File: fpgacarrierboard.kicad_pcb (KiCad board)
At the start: 6 copper layers, 150 x 100 mm, 211 parts, among them J1 Conn_01x06, J2 Conn_Coaxial, J3 HR911130C, J4 SFPK-SL, J5 Conn_02x10_Odd_Even, SW1 SW_Push, SW2 SW_Push, SW3 SW_Push, U1 TPS62130A, U2 TPS62130A, U3 TPS62130A, U4 TPS62130A, U5 TPS2592xx, U6 XC7A35T-FGG484, U7 W25Q128JVS, U8 RTL8211E-VB-CG, Y1 OT322550MJBA4SL, Y3 OT322525MJBA4SL

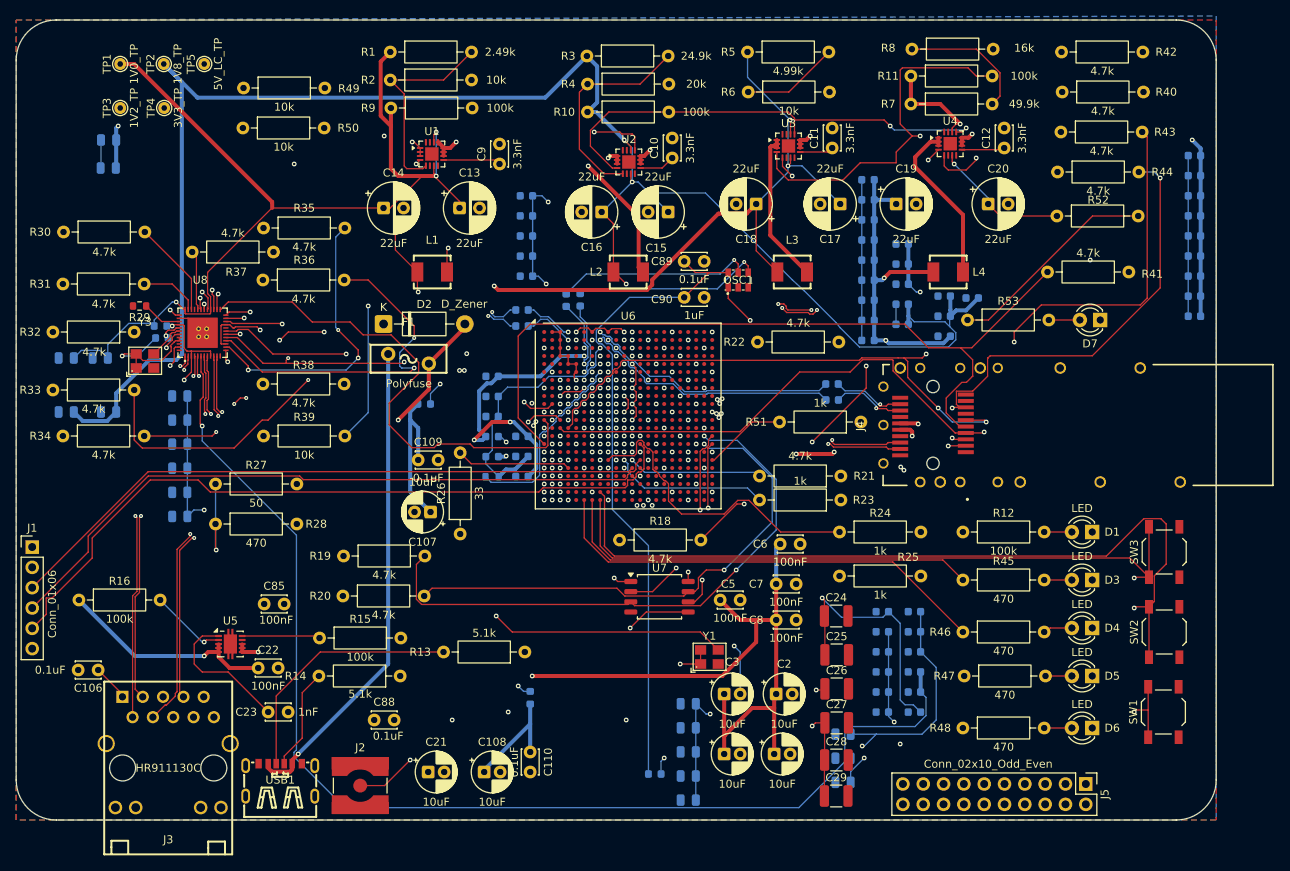
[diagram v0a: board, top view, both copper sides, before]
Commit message: As-ordered: fab outputs, JLC BOM/CPL, hand-solder BOM
- Gerbers and drill files (gerbers/), 6-layer, matching board saved 00:32
- bom_jlc.csv / gerbers/fpgacarrierboard-BOM.csv: 109 SMD parts for JLC
- gerbers/fpgacarrierboard-CPL.csv: placement for the same 109 parts
- bom_handsolder.csv: 97 through-hole parts plus SW1-SW3
- DRC: 0 errors, 0 unconnected, parity clean
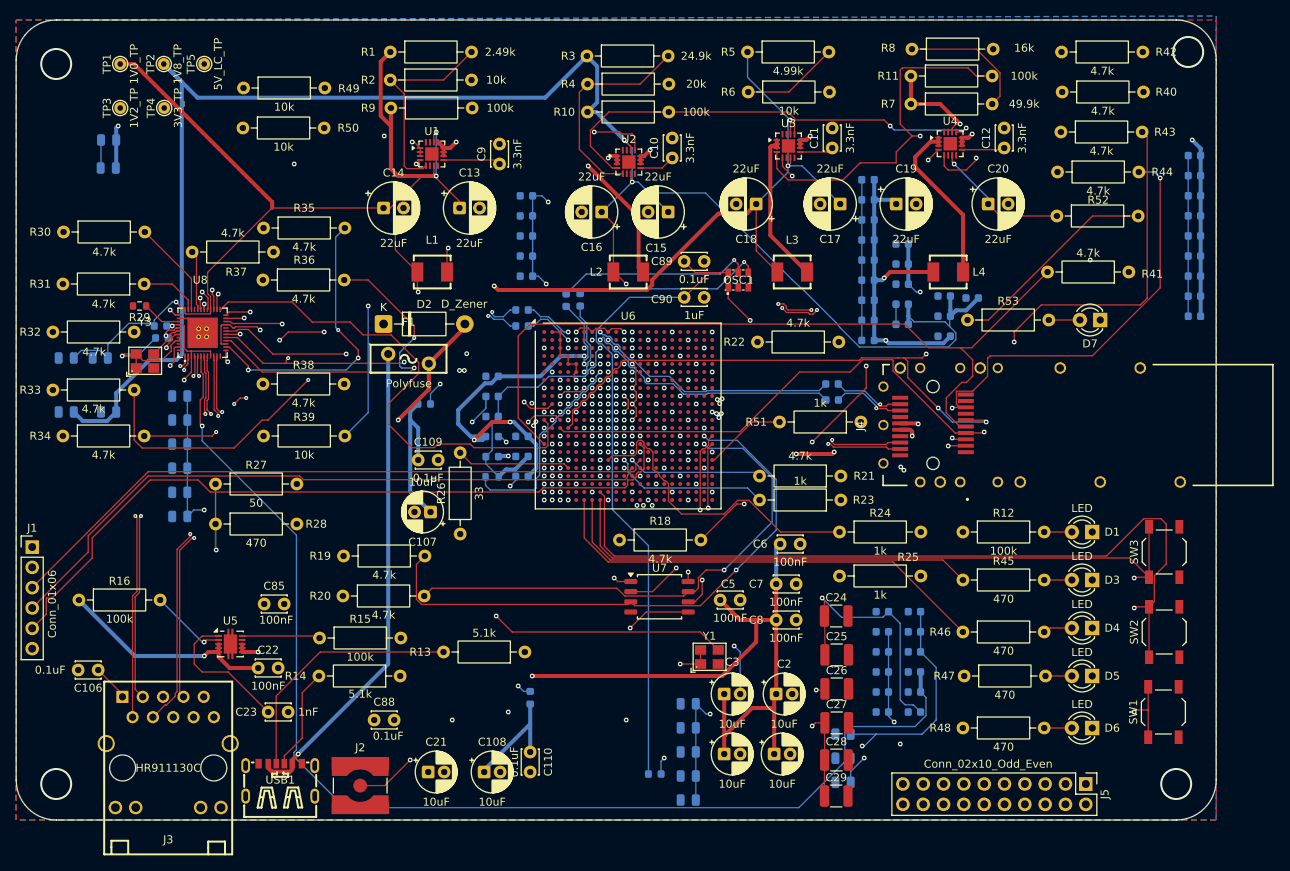
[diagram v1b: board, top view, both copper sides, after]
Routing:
- net GND: track 98.0 -> 117.3 mm, vias 109 -> 115
- net MGTAVCC: track 44.5 -> 48.0 mm
- net Net-(U6E-MGTRREF_216): track 24.8 -> 27.0 mm
- net 1V2: track 199.8 -> 200.3 mm
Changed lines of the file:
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@@
 			(outputformat 1)
 			(mirror no)
-			(drillshape 1)
+			(drillshape 0)
 			(scaleselection 1)
-			(outputdirectory "")
+			(outputdirectory "gerbers/")
 		)
 	)
@@
 	)
 	(via
-		(at 186.25 79)
+		(at 186.5 79)
 		(size 0.6)
 		(drill 0.3)
@@
 	)
 	(segment
-		(start 185.2775 79.08)
-		(end 186.17 79.08)
-		(width 0.5)
+		(start 221.475 43.525)
+		(end 217.5 47.5)
+		(width 0.15)
 		(layer "B.Cu")
 		(net "1V2")
 	)
 	(segment
-		(start 186.17 79.08)
-		(end 186.25 79)
+		(start 185.67 79)
+		(end 185.59 79.08)
 		(width 0.5)
 		(layer "B.Cu")
@@
 	)
 	(segment
-		(start 221.475 43.525)
-		(end 217.5 47.5)
-		(width 0.15)
-		(layer "B.Cu")
-		(net "1V2")
-	)
-	(segment
 		(start 221.75 37)
 		(end 216.42 31.67)
@@
 	)
 	(segment
+		(start 186.5 79)
+		(end 185.67 79)
+		(width 0.5)
+		(layer "B.Cu")
+		(net "1V2")
+	)
+	(segment
 		(start 221.475 37.275)
 		(end 221.75 37)
@@
 	)
 	(segment
+		(start 185.59 79.08)
+		(end 185.2775 79.08)
+		(width 0.5)
+		(layer "B.Cu")
+		(net "1V2")
+	)
+	(segment
 		(start 172.46005 73.8)
 		(end 177.111472 73.8)
@@
 	)
 	(segment
+		(start 186.5 79)
+		(end 183.26005 79)
+		(width 0.5)
+		(layer "In3.Cu")
+		(net "1V2")
+	)
+	(segment
 		(start 156.662943 54.7)
 		(end 158.011472 54.7)
@@
 	)
 	(segment
-		(start 183.26005 79)
-		(end 186.25 79)
-		(width 0.5)
-		(layer "In3.Cu")
-		(net "1V2")
-	)
-	(segment
 		(start 162.2 60.8)
 		(end 162.2 77.45)
@@
 	)
 	(segment
-		(start 182.755025 78.494975)
-		(end 183.26005 79)
-		(width 0.5)
-		(layer "In3.Cu")
-		(net "1V2")
-	)
-	(segment
 		(start 138 35.5)
 		(end 138 36.037057)
@@
 	)
 	(segment
+		(start 183.26005 79)
+		(end 182.755025 78.494975)
+		(width 0.5)
+		(layer "In3.Cu")
+		(net "1V2")
+	)
+	(segment
 		(start 199.41 63.09)
 		(end 200.59 63.09)
@@
 	)
 	(via
+		(at 130 120)
+		(size 4)
+		(drill 3.5)
+		(layers "F.Cu" "B.Cu")
+		(free yes)
+		(net "GND")
+	)
+	(via
 		(at 202 65.5)
 		(size 0.6)
@@
 	)
 	(via
+		(at 186.75 82.75)
+		(size 0.6)
+		(drill 0.3)
+		(layers "F.Cu" "B.Cu")
+		(net "GND")
+	)
+	(via
 		(at 199 72.5)
 		(size 0.6)
@@
 	)
 	(via
+		(at 182 74.75)
+		(size 0.6)
+		(drill 0.3)
+		(layers "F.Cu" "B.Cu")
+		(net "GND")
+	)
+	(via
 		(at 212.938203 72.445677)
 		(size 0.6)
@@
 	)
 	(via
+		(at 271.5 28.5)
+		(size 4)
+		(drill 3.5)
+		(layers "F.Cu" "B.Cu")
+		(free yes)
+		(net "GND")
+	)
+	(via
 		(at 198 69.5)
 		(size 0.6)
@@
 	)
 	(via
+		(at 130 30)
+		(size 4)
+		(drill 3.5)
+		(layers "F.Cu" "B.Cu")
+		(free yes)
+		(net "GND")
+	)
+	(via
 		(at 235.566378 80.3755)
 		(size 0.6)
@@
 	)
 	(via
+		(at 270 120)
+		(size 4)
+		(drill 3.5)
+		(layers "F.Cu" "B.Cu")
+		(free yes)
+		(net "GND")
+	)
+	(via
 		(at 200 75.5)
 		(size 0.6)
@@
 	)
 	(segment
+		(start 187.44 82.06)
+		(end 186.75 82.75)
+		(width 0.15)
+		(layer "B.Cu")
+		(net "GND")
+	)
+	(segment
+		(start 187.44 81.56)
+		(end 187.44 82.06)
+		(width 0.15)
+		(layer "B.Cu")
+		(net "GND")
+	)
+	(segment
 		(start 215.5 103.5)
 		(end 214.75 102.75)
@@
 	)
 	(segment
+		(start 183.715 71.55)
+		(end 183.715 73.035)
+		(width 0.15)
+		(layer "B.Cu")
+		(net "GND")
+	)
+	(segment
 		(start 271.5 61.53)
 		(end 271.5 41.45)
@@
 	)
 	(segment
+		(start 183.715 73.035)
+		(end 182 74.75)
+		(width 0.15)
+		(layer "B.Cu")
+		(net "GND")
+	)
+	(segment
+		(start 182 74.75)
+		(end 183.925 72.825)
+		(width 0.15)
+		(layer "In3.Cu")
+		(net "GND")
+	)
+	(segment
+		(start 183.925 72.825)
+		(end 189.0385 72.825)
+		(width 0.15)
+		(layer "In3.Cu")
+		(net "GND")
+	)
+	(segment
+		(start 189.0385 72.825)
+		(end 189.463 72.4005)
+		(width 0.15)
+		(layer "In3.Cu")
+		(net "GND")
+	)
+	(segment
 		(start 145.16 64.09)
 		(end 147.8 64.09)
@@
 	)
 	(segment
+		(start 191.525 83.025)
+		(end 192 83.5)
+		(width 0.15)
+		(layer "In4.Cu")
+		(net "GND")
+	)
+	(segment
+		(start 187.025 83.025)
+		(end 191.525 83.025)
+		(width 0.15)
+		(layer "In4.Cu")
+		(net "GND")
+	)
+	(segment
 		(start 201.25 112)
 		(end 187.5 112)
@@
 	)
 	(segment
+		(start 186.75 82.75)
+		(end 187.025 83.025)
+		(width 0.15)
+		(layer "In4.Cu")
+		(net "GND")
+	)
+	(segment
 		(start 150.6025 64.965)
 		(end 150.6275 64.99)
@@
 	)
 	(segment
-		(start 184.39 69.915)
-		(end 185.265 69.04)
-		(width 0.5)
-		(layer "B.Cu")
-		(net "MGTAVCC")
-	)
-	(segment
-		(start 182.865 70.885)
-		(end 183.835 69.915)
+		(start 181.82 76.57)
+		(end 180.25 75)
 		(width 0.5)
 		(layer "B.Cu")
@@
 	)
 	(segment
-		(start 182.865 75.7325)
-		(end 182.865 70.885)
+		(start 183.585 69.915)
+		(end 184.39 69.915)
 		(width 0.5)
 		(layer "B.Cu")
@@
 	)
 	(segment
+		(start 184.39 69.915)
+		(end 185.265 69.04)
+		(width 0.5)
+		(layer "B.Cu")
+		(net "MGTAVCC")
+	)
+	(segment
 		(start 190 77.55)
 		(end 188.99 76.54)
@@
 	)
 	(segment
+		(start 180.25 75)
+		(end 180.25 73.25)
+		(width 0.5)
+		(layer "B.Cu")
+		(net "MGTAVCC")
+	)
+	(segment
 		(start 190.540761 69.04)
 		(end 193.080761 66.5)
@@
 	)
 	(segment
-		(start 183.7025 76.57)
-		(end 182.865 75.7325)
+		(start 180.25 73.25)
+		(end 183.585 69.915)
 		(width 0.5)
 		(layer "B.Cu")
@@
 	)
 	(segment
-		(start 183.835 69.915)
-		(end 184.39 69.915)
+		(start 183.7025 76.57)
+		(end 181.82 76.57)
 		(width 0.5)
 		(layer "B.Cu")
@@
 	)
 	(segment
+		(start 183.665 81.59)
+		(end 183.665 82.665)
+		(width 0.15)
+		(layer "B.Cu")
+		(net "Net-(U6E-MGTRREF_216)")
+	)
+	(segment
 		(start 196.475 70.303248)
 		(end 196.803248 69.975)
@@
 	)
 	(segment
+		(start 183.665 82.665)
+		(end 184.25 83.25)
+		(width 0.15)
+		(layer "B.Cu")
+		(net "Net-(U6E-MGTRREF_216)")
+	)
+	(segment
 		(start 197.196752 69.975)
 		(end 197.475 69.696752)
@@
 	)
 	(segment
-		(start 189.538248 82.29)
+		(start 190 81.828248)
 		(end 190.425 81.403248)
 		(width 0.15)
@@
 	)
 	(segment
+		(start 189.75 83.25)
+		(end 190 83)
+		(width 0.15)
+		(layer "B.Cu")
+		(net "Net-(U6E-MGTRREF_216)")
+	)
+	(segment
 		(start 191.196752 75.975)
 		(end 192.475 74.696752)
@@
 	)
 	(segment
+		(start 190 83)
+		(end 190 81.828248)
+		(width 0.15)
+		(layer "B.Cu")
+		(net "Net-(U6E-MGTRREF_216)")
+	)
+	(segment
 		(start 196.803248 69.975)
 		(end 197.196752 69.975)
@@
 	)
 	(segment
-		(start 183.665 81.59)
-		(end 184.365 82.29)
+		(start 184.25 83.25)
+		(end 189.75 83.25)
 		(width 0.15)
 		(layer "B.Cu")
@@
 		(width 0.15)
 		(layer "B.Cu")
-		(net "Net-(U6E-MGTRREF_216)")
-	)
-	(segment
-		(start 184.365 82.29)
-		(end 189.538248 82.29)
-		(width 0.15)
-		(layer "B.Cu")
